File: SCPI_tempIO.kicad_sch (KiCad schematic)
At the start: 19 parts, among them J1 Conn_ARM_JTAG_SWD_10, J2 Conn_02x05_Odd_Even, P1 USB_C_Plug_USB2.0, SW1 SW_SPST, U1 STM32G070KBTx, U2 AP2112K-3.3, U3 SHT4x

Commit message: USB for contemporary goodness
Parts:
- removed P1: USB_C_Plug_USB2.0, symbol Connector:USB_C_Plug_USB2.0
- added D1: LED, LED_SMD:LED_01005_0402Metric_Pad0.57x0.30mm_HandSolder, symbol Device:LED
- added J3: USB_C_Receptacle_USB2.0_14P, symbol Connector:USB_C_Receptacle_USB2.0_14P
- added R10, R11: 5.1k, Resistor_SMD:R_0402_1005Metric, symbol Device:R
- added R12, R13: 22, Resistor_SMD:R_0402_1005Metric, symbol Device:R
- added R9: 1000, Resistor_SMD:R_0402_1005Metric, symbol Device:R
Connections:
- net GND: now also D1.1 (K), J3.A1 (GND), J3.A12 (GND), J3.B1 (GND), J3.B12 (GND), J3.SH (SHIELD), R10.2, R11.2
- net at R6.1: now also U1.13 (PA6)
- net at R4.1: now also U1.10 (PA3)
- net 3v3: now reaches C1.1, C2.1, J2.1 (Pin_1), U1.4 (VDD), U2.5 (VOUT), U3.3 (VDD)
- net at R2.1: now also U1.8 (PA1)
- net at U1.11 (PA4): now also R5.1
- net at U1.12 (PA5): now also R8.1
- net at U1.14 (PA7): now also R7.1
- net USBD-: now reaches U1.22 (PA9/PA11)
- net USBD-: now also R12.2
- net USBD+: now reaches U1.23 (PA10/PA12)
- net USBD+: now also R13.2
- net at U1.26 (PA15): now also R9.1
- net at U1.30 (PB6): now also U3.2 (SCL)
- net at U1.31 (PB7): now also U3.1 (SDA)
- net at U1.7 (PA0): now also R1.1
- net at U1.9 (PA2): now also R3.1
- net at C3.1, J1.1 (VTref), U2.1 (VIN)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: now also J3.A4 (VBUS), J3.A9 (VBUS), J3.B4 (VBUS), J3.B9 (VBUS)
- new net: J3.B5 (CC2), R10.1
- new net: J3.A7 (D-), J3.B7 (D-), R12.1
- new net: J3.A5 (CC1), R11.1
- new net: J3.A6 (D+), J3.B6 (D+), R13.1
- new net: D1.2 (A), R9.2
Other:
- moved on the sheet: C1, C2, C3, C4, J1, J2, R1, R2, R3, R4, R5, R6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

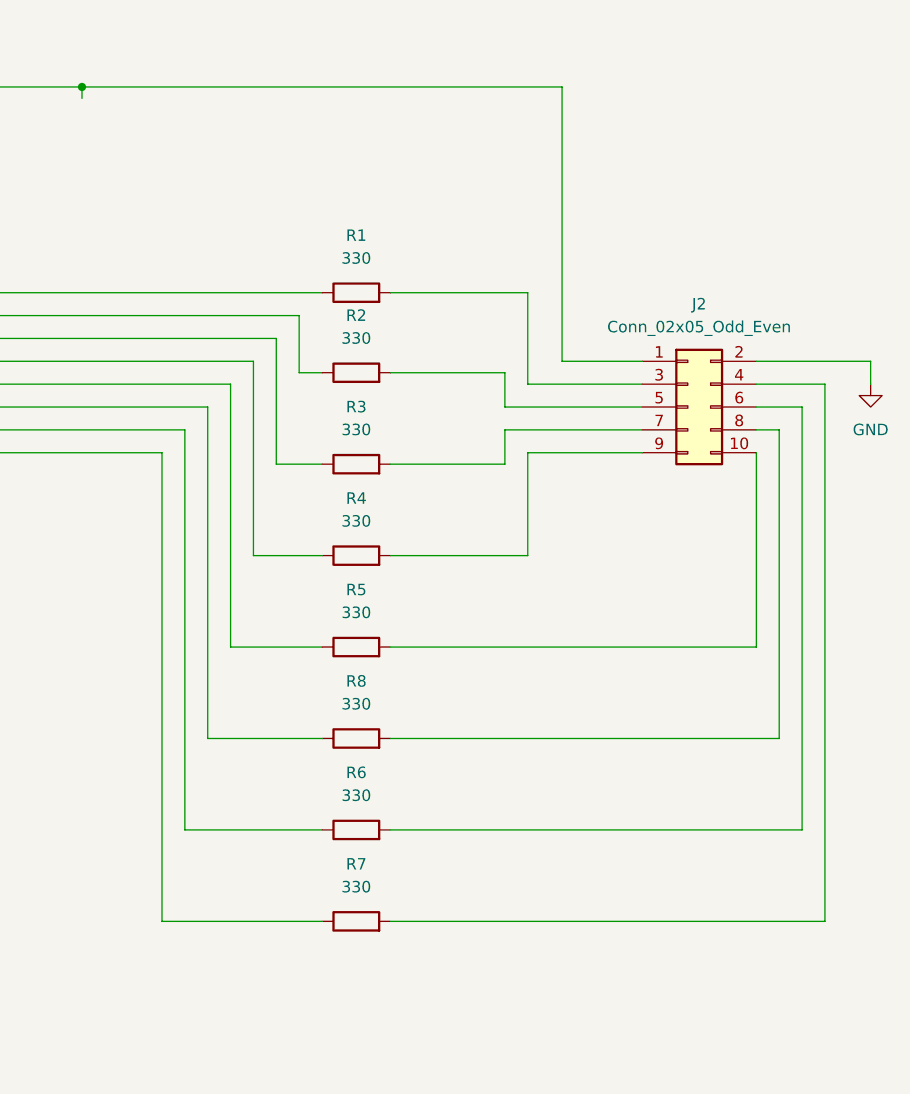
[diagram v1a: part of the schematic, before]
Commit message: assigned gpio r footprints
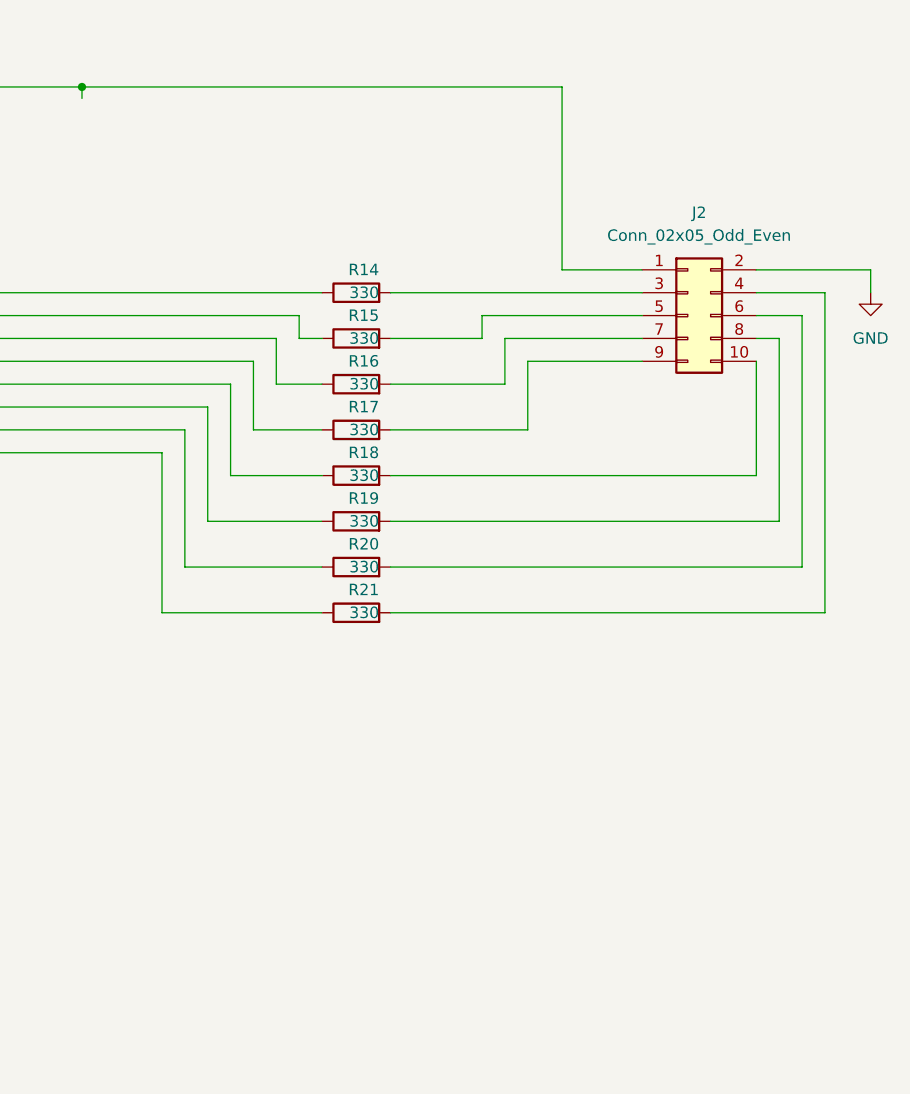
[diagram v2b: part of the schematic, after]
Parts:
- removed R1, R2, R3, R4, R5, R6, R7, R8: 330, symbol Device:R
- added R14, R15, R16, R17, R18, R19, R20, R21: 330, Resistor_SMD:R_0402_1005Metric, symbol Device:R
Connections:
- net at U1.13 (PA6): now also R20.1
- net at J2.6 (Pin_6): now also R20.2
- net at U1.10 (PA3): now also R17.1
- net at J2.9 (Pin_9): now also R17.2
- net at U1.8 (PA1): now also R15.1
- net at J2.5 (Pin_5): now also R15.2
- net at U1.11 (PA4): now also R18.1
- net at U1.12 (PA5): now also R19.1
- net at U1.14 (PA7): now also R21.1
- net at U1.7 (PA0): now also R14.1
- net at U1.9 (PA2): now also R16.1
- net at J2.4 (Pin_4): now also R21.2
- net at J2.8 (Pin_8): now also R19.2
- net at J2.10 (Pin_10): now also R18.2
- net at J2.3 (Pin_3): now also R14.2
- net at J2.7 (Pin_7): now also R16.2
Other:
- moved on the sheet: J2

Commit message: PCB BABY
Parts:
- removed C1, C4: 100n, symbol Device:C
- removed C2: 4.7n, symbol Device:C
- removed C3: 1u, symbol Device:C
- removed J2: Conn_02x05_Odd_Even, symbol Connector_Generic:Conn_02x05_Odd_Even
- added C5, C6: 100n, Capacitor_SMD:C_0805_2012Metric, symbol Device:C
- added C7: 1u, Capacitor_SMD:C_0805_2012Metric, symbol Device:C
- added C8: 4.7n, Capacitor_SMD:C_0805_2012Metric, symbol Device:C
- added J2: Conn_02x05_Counter_Clockwise, Connector_IDC:IDC-Header_2x05_P2.54mm_Vertical, symbol Connector_Generic:Conn_02x05_Counter_Clockwise
- added J4, J5: Conn_01x04_Pin, Connector_PinSocket_1.00mm:PinSocket_1x04_P1.00mm_Vertical, symbol Connector:Conn_01x04_Pin
- J3: footprint (none) -> Connector_USB:USB_C_Receptacle_HRO_TYPE-C-31-M-12
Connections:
- net 3v3: now also C6.1, C8.1, J2.1 (Pin_1), J4.1 (Pin_1), J5.1 (Pin_1)
- net GND: now also C5.2, C6.2, C7.2, C8.2, J2.10 (Pin_10), J4.4 (Pin_4), J5.4 (Pin_4)
- net at J1.10 (~{RESET}), SW1.1 (A), U1.6 (NRST): now also C5.1
- net at U1.30 (PB6), U3.2 (SCL): now also J4.2 (Pin_2), J5.2 (Pin_2)
- net at U1.31 (PB7), U3.1 (SDA): now also J4.3 (Pin_3), J5.3 (Pin_3)
- net at R15.2: now also J2.3 (Pin_3)
- net at R17.2: now also J2.5 (Pin_5)
- net at R18.2: now also J2.6 (Pin_6)
- net at R16.2: now also J2.4 (Pin_4)
- net at J1.1 (VTref), J3.A4 (VBUS), J3.A9 (VBUS)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: now also C7.1
- net at R20.2: now also J2.8 (Pin_8)
- net at R14.2: now also J2.2 (Pin_2)
- net at R21.2: now also J2.9 (Pin_9)
- net at R19.2: now also J2.7 (Pin_7)
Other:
- moved on the sheet: U3

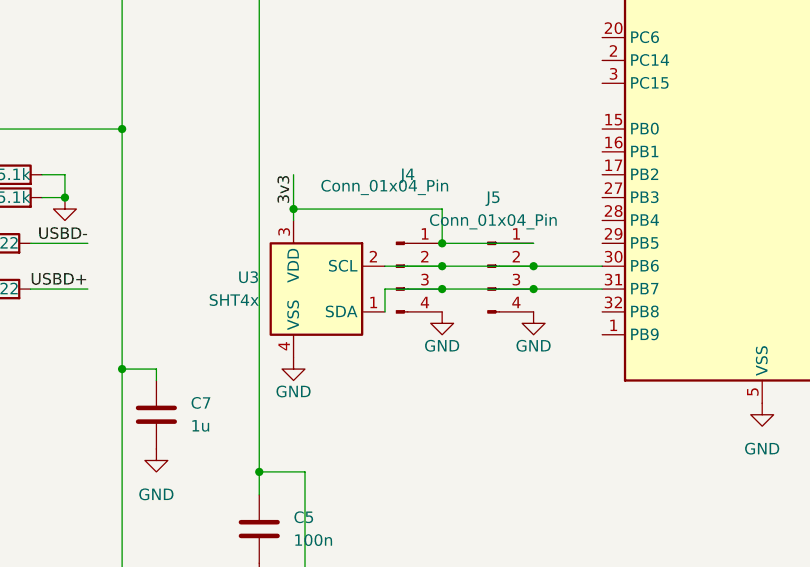
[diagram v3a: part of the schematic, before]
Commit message: pullups and cap for the SHT4x
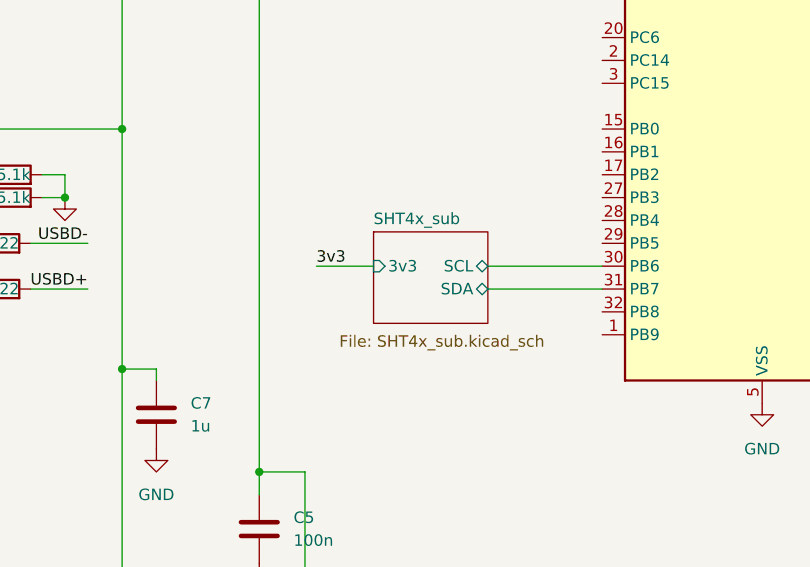
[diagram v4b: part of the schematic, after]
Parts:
- removed J4, J5: Conn_01x04_Pin, Connector_PinSocket_1.00mm:PinSocket_1x04_P1.00mm_Vertical, symbol Connector:Conn_01x04_Pin
- removed U3: SHT4x, Sensor_Humidity:Sensirion_DFN-4_1.5x1.5mm_P0.8mm_SHT4x_NoCentralPad, symbol Sensor_Humidity:SHT4x
- D1: footprint LED_SMD:LED_01005_0402Metric_Pad0.57x0.30mm_HandSolder -> LED_SMD:LED_0402_1005Metric
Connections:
- net SHT4x_sub/SCL: now reaches U1.30 (PB6)
- net SHT4x_sub/SDA: now reaches U1.31 (PB7)
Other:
- added sheet SHT4x_sub (SHT4x_sub.kicad_sch)

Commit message: sent to JLC noodleUSBp16
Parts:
- removed J3: USB_C_Receptacle_USB2.0_14P, Connector_USB:USB_C_Receptacle_HRO_TYPE-C-31-M-12, symbol Connector:USB_C_Receptacle_USB2.0_14P
- added J3: USB_C_Receptacle_USB2.0_16P, Connector_USB:USB_C_Receptacle_G-Switch_GT-USB-7025, symbol Connector:USB_C_Receptacle_USB2.0_16P
- U1: value STM32G070KBTx -> STM32G0B1KBT6
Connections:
- net GND: now also J3.A1 (GND), J3.A12 (GND), J3.B1 (GND), J3.B12 (GND), J3.SH (SHIELD)
- net at R10.1: now also J3.B5 (CC2)
- net at C7.1, J1.1 (VTref), U2.1 (VIN)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: now also J3.A4 (VBUS), J3.A9 (VBUS), J3.B4 (VBUS), J3.B9 (VBUS)
- net at R12.1: now also J3.A7 (D-), J3.B7 (D-)
- net at R11.1: now also J3.A5 (CC1)
- net at R13.1: now also J3.A6 (D+), J3.B6 (D+)
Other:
- note added: "C5,C6,C9 C49678 100n 0805 C7 C28323 1u 0805 C8 C1744 4.7n 0805 D1 C965793 LED 0402 J1 C2935458 Conn_ARM_JTAG_SWD_10 PinHeader_2x05_P1.27mm_Vertical_SMD J3 C963213 USB_C_Receptacle_USB2.0_16P USB_C_Receptacle_G-Switch_GT-USB-7025 R9 C11702 1000 0402 R10,R11 C25905 5.1k 0402 R12,R13 C25092 22 0402 R14,R15,R16,R17,R18,R19,R20,R21 C25104 330 0402 R23,R24 C25744 10k 0402 SW1 C10852 SW_SPST SW_Push_1P1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"
- moved on the sheet: C5
